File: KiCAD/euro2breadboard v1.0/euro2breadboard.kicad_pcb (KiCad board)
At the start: 2 copper layers, 33 x 53.3 mm, 13 parts, among them J1 JST_BUS, J2 IDC_BUS, SW1 SW_DPDT_x2

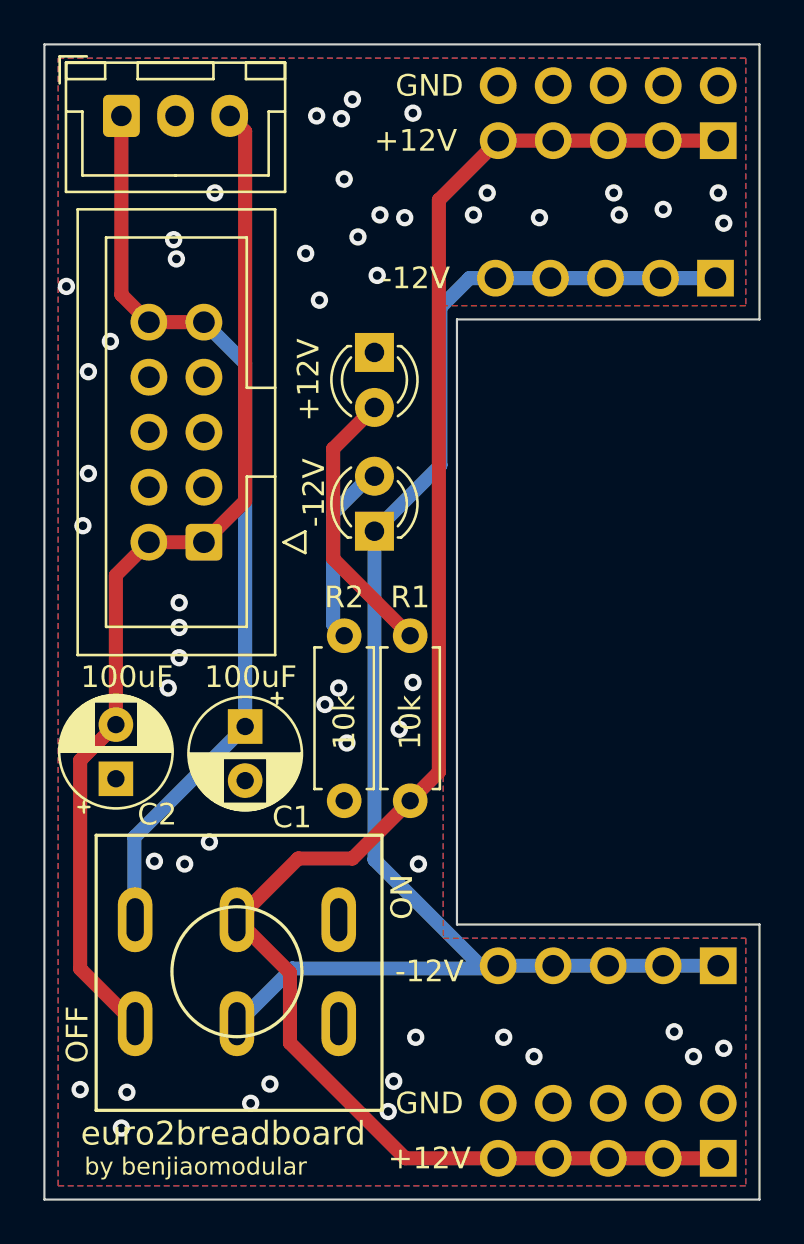
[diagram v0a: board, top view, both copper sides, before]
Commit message: Fixed board dimensions
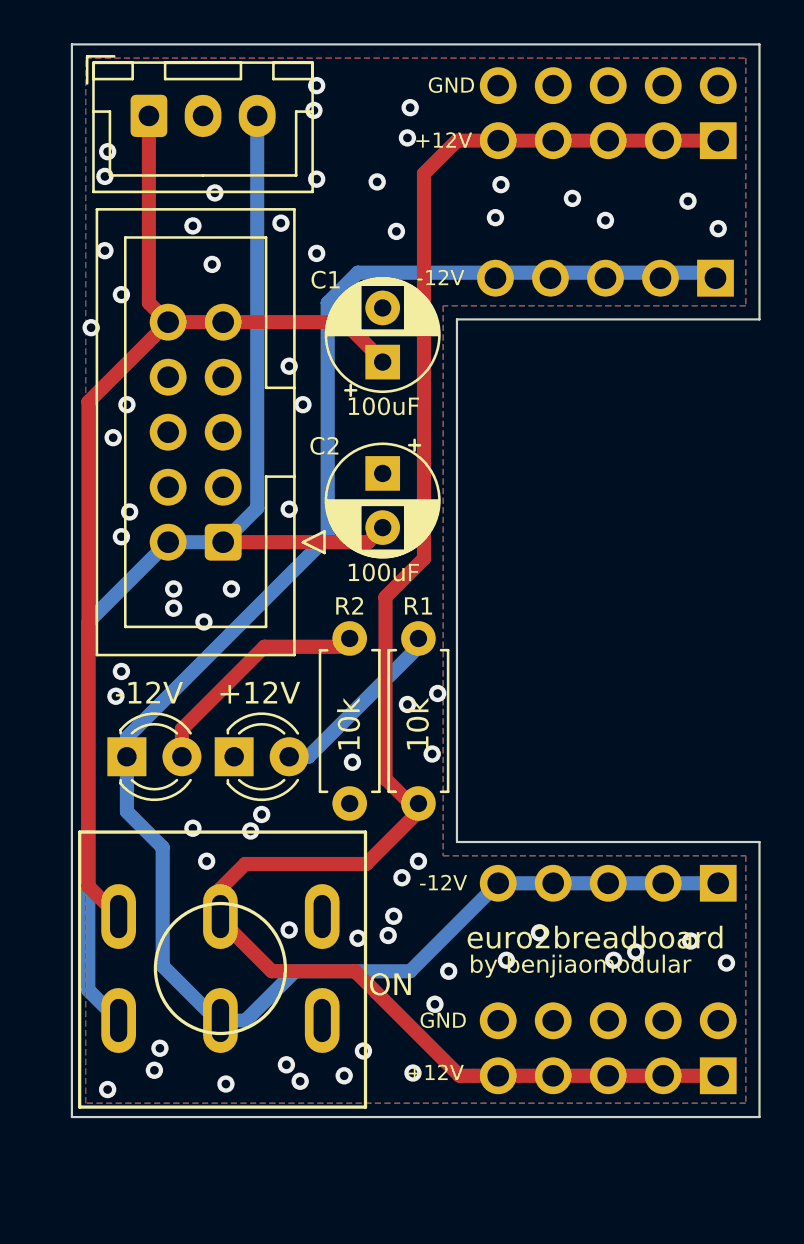
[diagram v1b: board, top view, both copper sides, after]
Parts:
- moved +12V 19.8 mm to (76.1, 72.9), turned to 0 degrees
- moved C2 18.7 mm to (82.9, 59.8), turned to 270 degrees
- moved C1 18.0 mm to (82.9, 54.7), turned to 90 degrees
- moved -12V 15.5 mm to (71.1, 72.9), turned to 0 degrees
- moved BB_POWER_PINS1 3.81 mm to (98.4, 87.6)
- moved NEG_12V_PINS2 3.81 mm to (98.4, 78.7)
- moved J1 1.27 mm to (72.1, 43.3)
- moved J2 0.89 mm to (75.6, 63.0)
- moved SW1 0.78 mm to (75.4, 82.7)
- moved R1 0.40 mm to (84.6, 67.4)
- moved R2 0.28 mm to (81.4, 67.4)
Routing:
- net Net-(NEG_12V_LED1-Pad1): track 71.1 -> 83.1 mm
- net +12V: track 43.1 -> 50.1 mm
- net -12V: track 47.9 -> 54.7 mm
- net Net-(POS_12V_LED1-Pad2): track 12.8 -> 8.07 mm
- net Net-(NEG_12V_LED1-Pad2): track 8.49 -> 10.7 mm
- net Net-(BB_POWER_PINS1-Pad1): track 81.3 -> 83.1 mm
- net GND: vias 53 -> 67
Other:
- board size 33 x 53.3 mm -> 31.8 x 49.5 mm
- board text removed: "OFF"
